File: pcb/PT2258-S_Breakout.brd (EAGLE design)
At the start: 75 x 50 mm, 41 parts, among them U1 PT2258-S, X1 INPUT, X2 I2C, X3 POWER, X4 OUTPUT

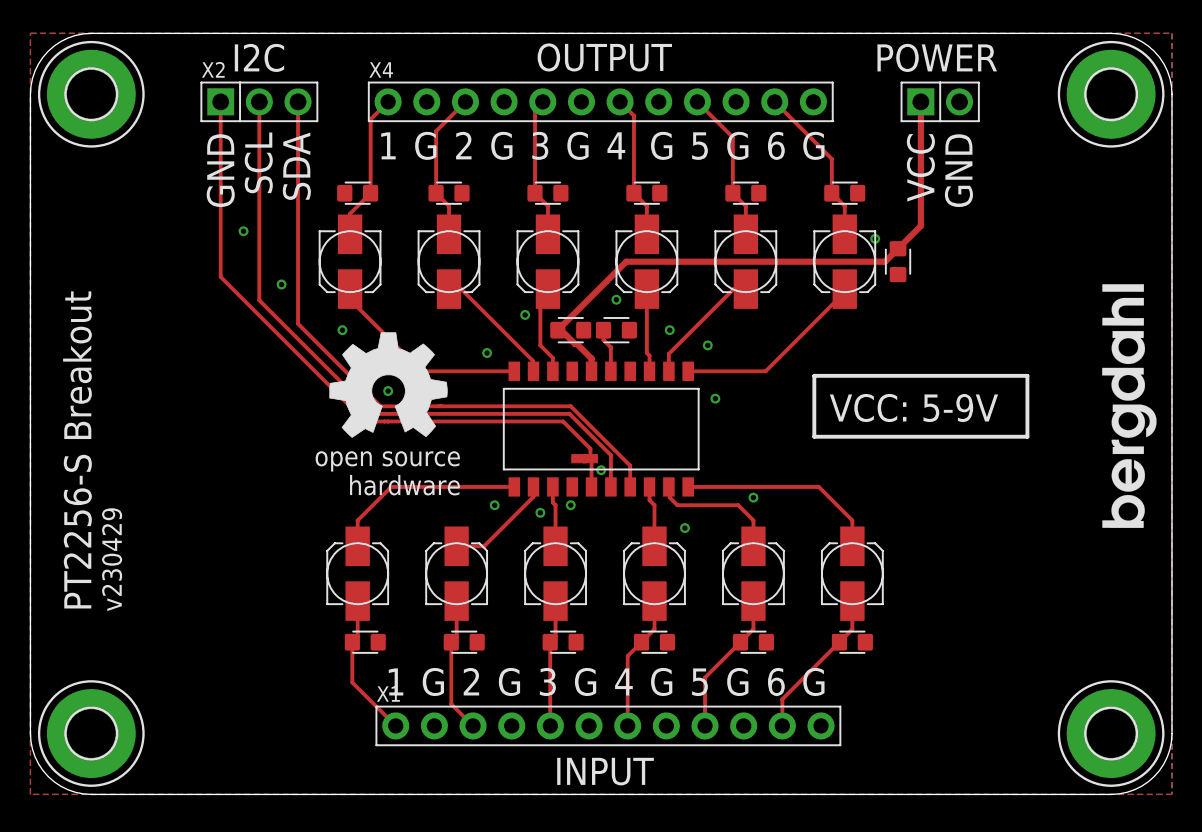
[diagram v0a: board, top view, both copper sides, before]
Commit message: Fix SOP-20-300 footprint
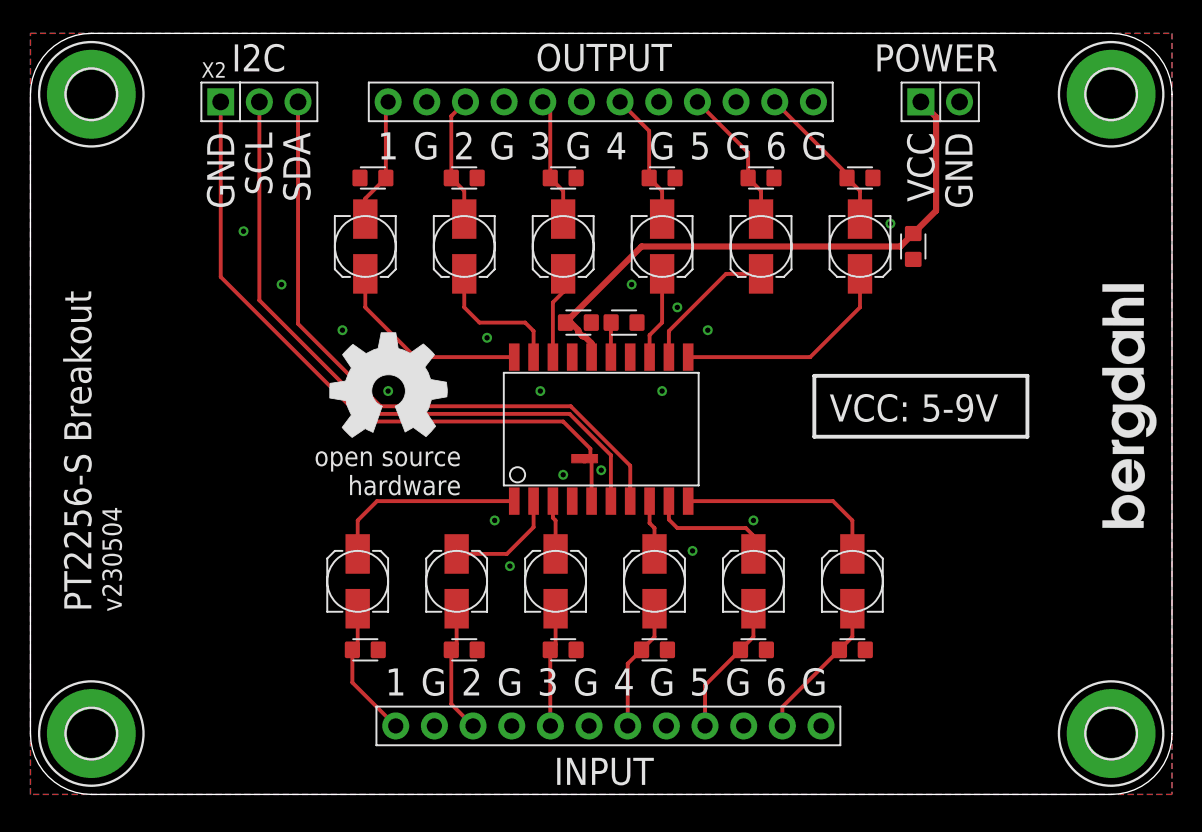
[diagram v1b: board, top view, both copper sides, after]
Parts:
- U1: device M2M-IC:SOP-20 -> M2M-IC:SOP-20-300
- moved C10 1.41 mm to (22.0, 36.0)
- moved C11 1.41 mm to (28.5, 36.0)
- moved C12 1.41 mm to (35.0, 36.0)
- moved C13 1.41 mm to (41.5, 36.0)
- moved C14 1.41 mm to (48.0, 36.0)
- moved C15 1.41 mm to (54.5, 36.0)
- moved C7 1.41 mm to (58.0, 36.0)
- moved R10 1.41 mm to (41.5, 40.5)
- moved R11 1.41 mm to (48.0, 40.5)
- moved R12 1.41 mm to (54.5, 40.5)
- moved R7 1.41 mm to (22.5, 40.5)
- moved R8 1.41 mm to (28.5, 40.5)
- moved R9 1.41 mm to (35.0, 40.5)
- moved U$2 1.41 mm to (38.0, 39.5)
- moved C8 0.71 mm to (39.0, 31.0)
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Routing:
- net N$9: track 12.6 -> 14.8 mm
- net N$2: track 9.85 -> 8.44 mm
- net N$1: track 9.74 -> 8.32 mm
- net N$10: track 7.96 -> 9.33 mm
- net N$3: track 9.26 -> 8.26 mm
- net N$13: track 8.17 -> 9.11 mm
- net SCL: track 42.4 -> 43.4 mm
- net GND: track 43.0 -> 43.9 mm
- net SDA: track 41.7 -> 42.6 mm
- net N$15: track 2.90 -> 2.28 mm
- net N$6: track 10.6 -> 10.0 mm
- net N$5: track 10.0 -> 9.43 mm
- net N$4: track 9.43 -> 8.84 mm
- net N$25: track 10.1 -> 9.61 mm
- net N$24: track 9.52 -> 9.02 mm
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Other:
- board text added: "v230504"
- board text removed: "v230429"
